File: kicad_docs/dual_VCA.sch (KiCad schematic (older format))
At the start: 18 parts, among them J1 signal_in_1, J2 CV_in_1, J3 signal_in_2, J4 CV_in_2, J5 signal_out_1, J6 signal_out_2, J8 Conn_01x06, J9 Conn_01x06

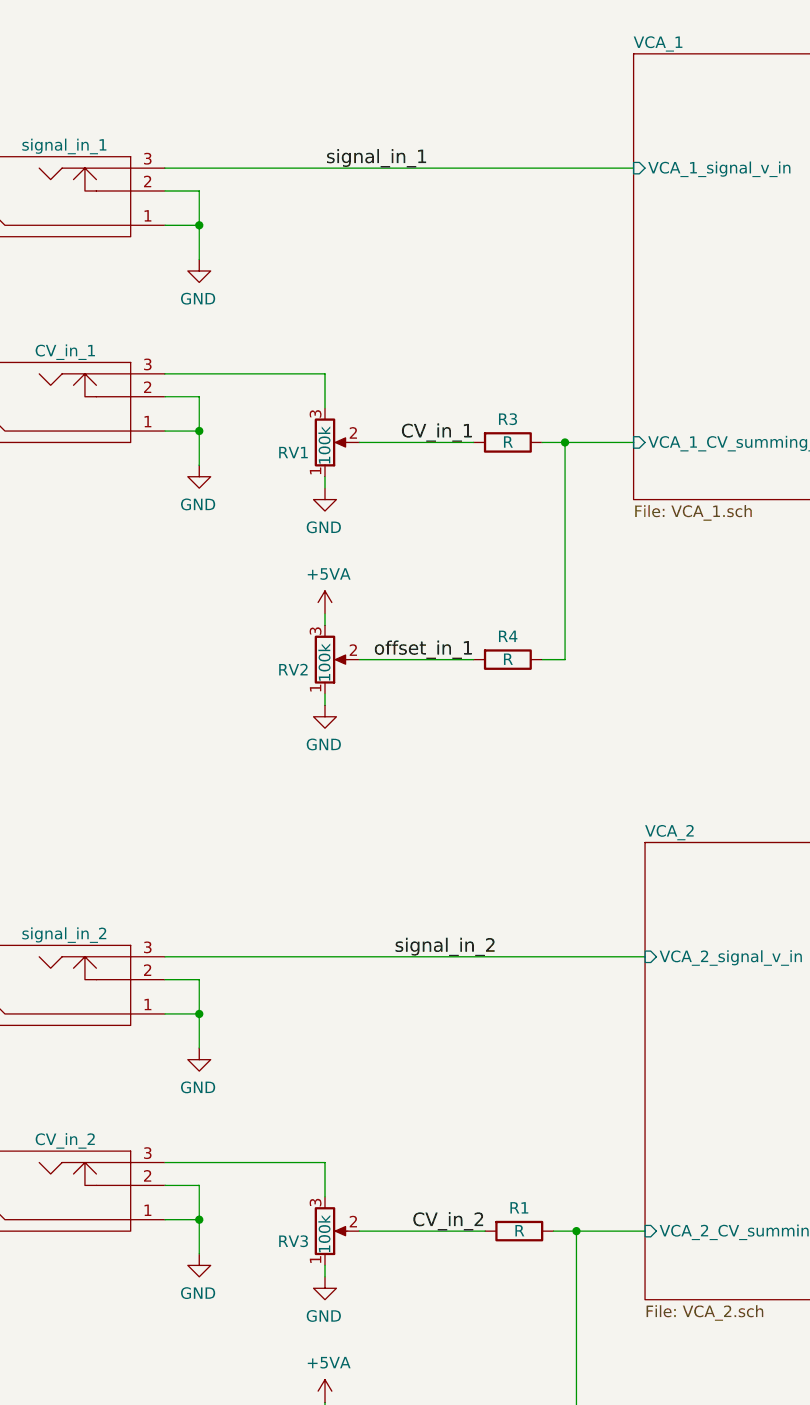
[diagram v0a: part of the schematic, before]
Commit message: add AC/DC coupling caps and jumper
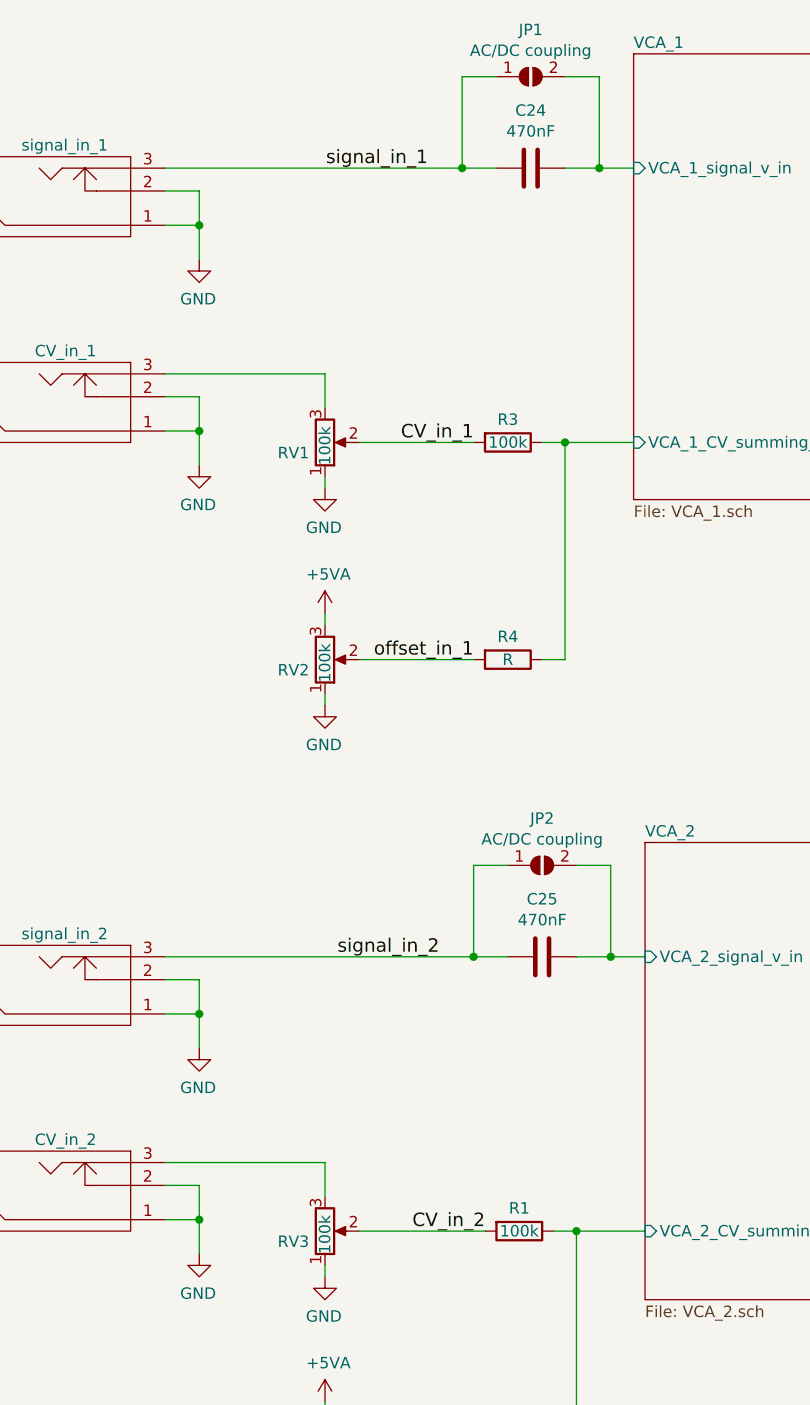
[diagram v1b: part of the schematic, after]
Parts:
- added C24, C25: 470nF, Capacitor_THT:C_Rect_L7.2mm_W3.5mm_P5.00mm_FKS2_FKP2_MKS2_MKP2, symbol Device:C
- added JP1, JP2: AC/DC coupling, Jumper:SolderJumper-2_P1.3mm_Open_RoundedPad1.0x1.5mm, symbol Jumper:SolderJumper_2_Open
- R1, R3: value R -> 100k
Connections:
- net signal_in_1: now also C24.2, JP1.1 (A)
- net signal_in_2: now also C25.2, JP2.1 (A)
- new net VCA_1/VCA_1_signal_v_in: C24.1, JP1.2 (B)
- new net VCA_2/VCA_2_signal_v_in: C25.1, JP2.2 (B)
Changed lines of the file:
@@
 Wire Wire Line
 	1700 5550 2400 5550
-Wire Wire Line
-	1700 4650 3800 4650
 $Comp
 L Device:R R1
@@
 P 3250 5850
 F 0 "R1" V 3150 5850 50  0000 C CNN
-F 1 "R" V 3250 5850 50  0000 C CNN
+F 1 "100k" V 3250 5850 50  0000 C CNN
 F 2 "Resistor_SMD:R_0805_2012Metric_Pad1.15x1.40mm_HandSolder" V 3180 5850 50  0001 C CNN
 F 3 "~" H 3250 5850 50  0001 C CNN
@@
 Wire Wire Line
 	2400 2100 2400 2250
-Wire Wire Line
-	1700 1200 3750 1200
 $Comp
 L Device:R R3
@@
 P 3200 2400
 F 0 "R3" V 3100 2400 50  0000 C CNN
-F 1 "R" V 3200 2400 50  0000 C CNN
+F 1 "100k" V 3200 2400 50  0000 C CNN
 F 2 "Resistor_SMD:R_0805_2012Metric_Pad1.15x1.40mm_HandSolder" V 3130 2400 50  0001 C CNN
 F 3 "~" H 3200 2400 50  0001 C CNN
@@
 Text Label 10250 1050 2    59   ~ 0
 signal_in_1
-Text Label 10250 1250 2    59   ~ 0
-CV_in_1
 Text Label 10250 1350 2    59   ~ 0
 offset_in_1
-Text Label 10250 1150 2    59   ~ 0
-signal_out_1
 $Comp
 L Connector_Generic:Conn_01x06 J9
@@
 Text Label 6750 1200 2    59   ~ 0
 signal_out_1
-Text Label 3150 4650 2    59   ~ 0
+Text Label 2900 4650 2    59   ~ 0
 signal_in_2
 Text Label 3100 5850 2    59   ~ 0
@@
 Wire Wire Line
 	6200 4650 6850 4650
+$Comp
+L Device:C C24
+U 1 1 5E401C22
+P 3300 1200
+F 0 "C24" V 3048 1200 50  0000 C CNN
+F 1 "470nF" V 3139 1200 50  0000 C CNN
+F 2 "Capacitor_THT:C_Rect_L7.2mm_W3.5mm_P5.00mm_FKS2_FKP2_MKS2_MKP2" H 3338 1050 50  0001 C CNN
+F 3 "~" H 3300 1200 50  0001 C CNN
+	1    3300 1200
+	0    1    1    0
+$EndComp
+Wire Wire Line
+	3450 1200 3600 1200
+Wire Wire Line
+	3150 1200 3000 1200
+$Comp
+L Jumper:SolderJumper_2_Open JP1
+U 1 1 5E4046A9
+P 3300 800
+F 0 "JP1" H 3300 1005 50  0000 C CNN
+F 1 "AC/DC coupling" H 3300 914 50  0000 C CNN
+F 2 "Jumper:SolderJumper-2_P1.3mm_Open_RoundedPad1.0x1.5mm" H 3300 800 50  0001 C CNN
+F 3 "~" H 3300 800 50  0001 C CNN
+	1    3300 800
+	1    0    0    -1
+$EndComp
+Wire Wire Line
+	3150 800  3000 800
+Wire Wire Line
+	3000 800  3000 1200
+Connection ~ 3000 1200
+Wire Wire Line
+	3000 1200 1700 1200
+Wire Wire Line
+	3450 800  3600 800
+Wire Wire Line
+	3600 800  3600 1200
+Connection ~ 3600 1200
+Wire Wire Line
+	3600 1200 3750 1200
+$Comp
+L Device:C C25
+U 1 1 5E409E9E
+P 3350 4650
+F 0 "C25" V 3098 4650 50  0000 C CNN
+F 1 "470nF" V 3189 4650 50  0000 C CNN
+F 2 "Capacitor_THT:C_Rect_L7.2mm_W3.5mm_P5.00mm_FKS2_FKP2_MKS2_MKP2" H 3388 4500 50  0001 C CNN
+F 3 "~" H 3350 4650 50  0001 C CNN
+	1    3350 4650
+	0    1    1    0
+$EndComp
+Wire Wire Line
+	3500 4650 3650 4650
+Wire Wire Line
+	3200 4650 3050 4650
+$Comp
+L Jumper:SolderJumper_2_Open JP2
+U 1 1 5E409EA6
+P 3350 4250
+F 0 "JP2" H 3350 4455 50  0000 C CNN
+F 1 "AC/DC coupling" H 3350 4364 50  0000 C CNN
+F 2 "Jumper:SolderJumper-2_P1.3mm_Open_RoundedPad1.0x1.5mm" H 3350 4250 50  0001 C CNN
+F 3 "~" H 3350 4250 50  0001 C CNN
+	1    3350 4250
+	1    0    0    -1
+$EndComp
+Wire Wire Line
+	3200 4250 3050 4250
+Wire Wire Line
+	3050 4250 3050 4650
+Connection ~ 3050 4650
+Wire Wire Line
+	3050 4650 1700 4650
+Wire Wire Line
+	3500 4250 3650 4250
+Wire Wire Line
+	3650 4250 3650 4650
+Connection ~ 3650 4650
+Wire Wire Line
+	3650 4650 3800 4650
+Text Label 10250 1250 2    59   ~ 0
+CV_in_1
+Text Label 10250 1150 2    59   ~ 0
+signal_out_1
 $EndSCHEMATC

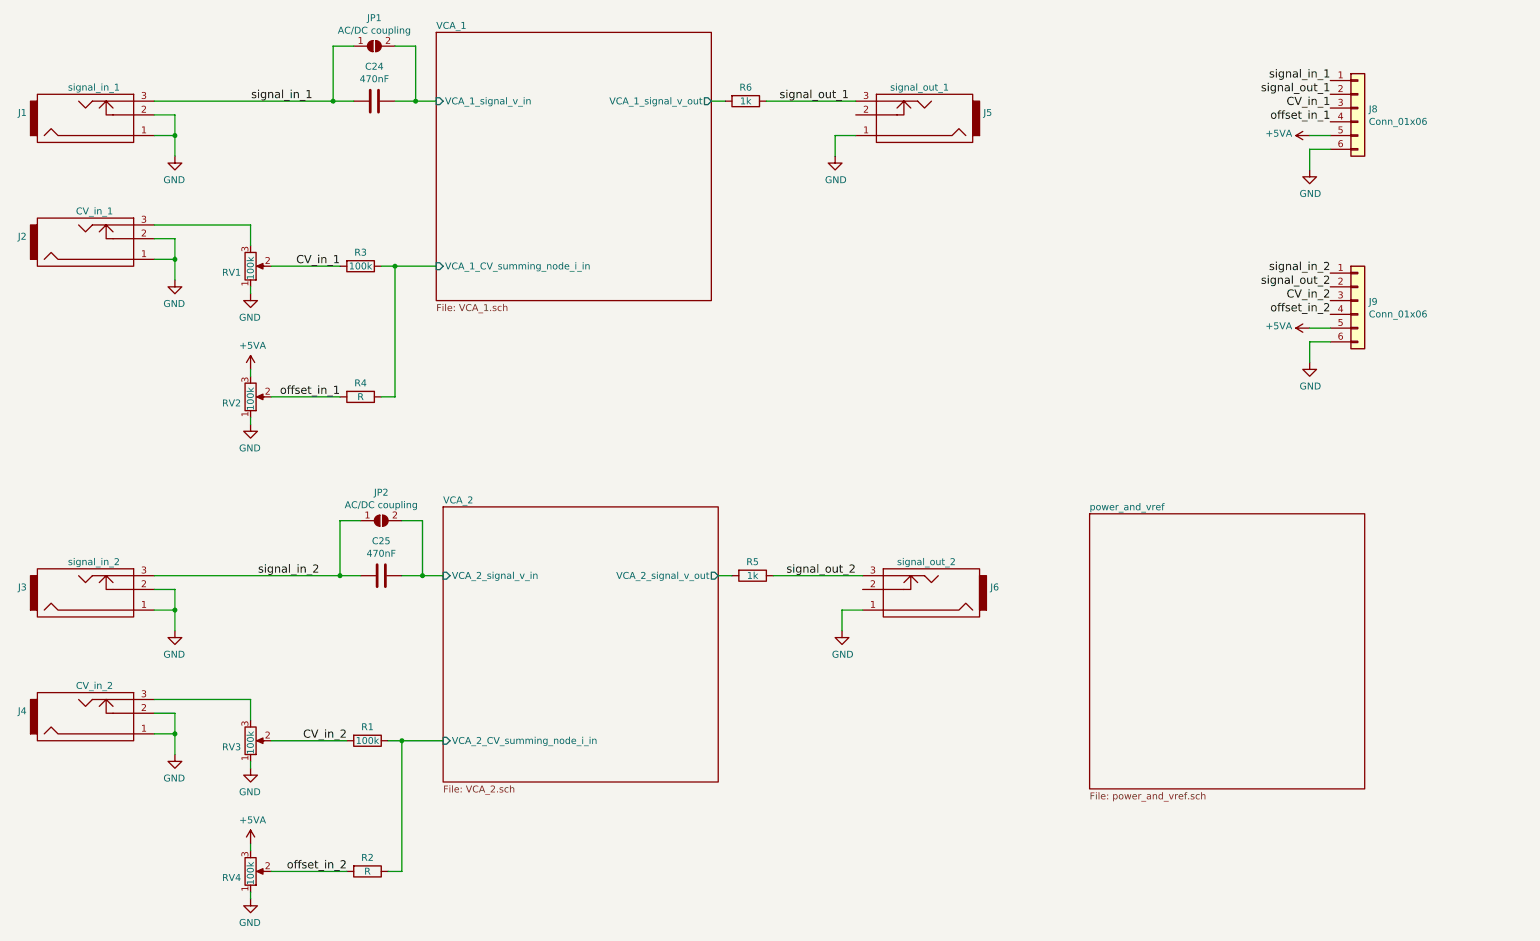
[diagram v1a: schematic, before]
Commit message: add values to r's, add r's to CV circuit
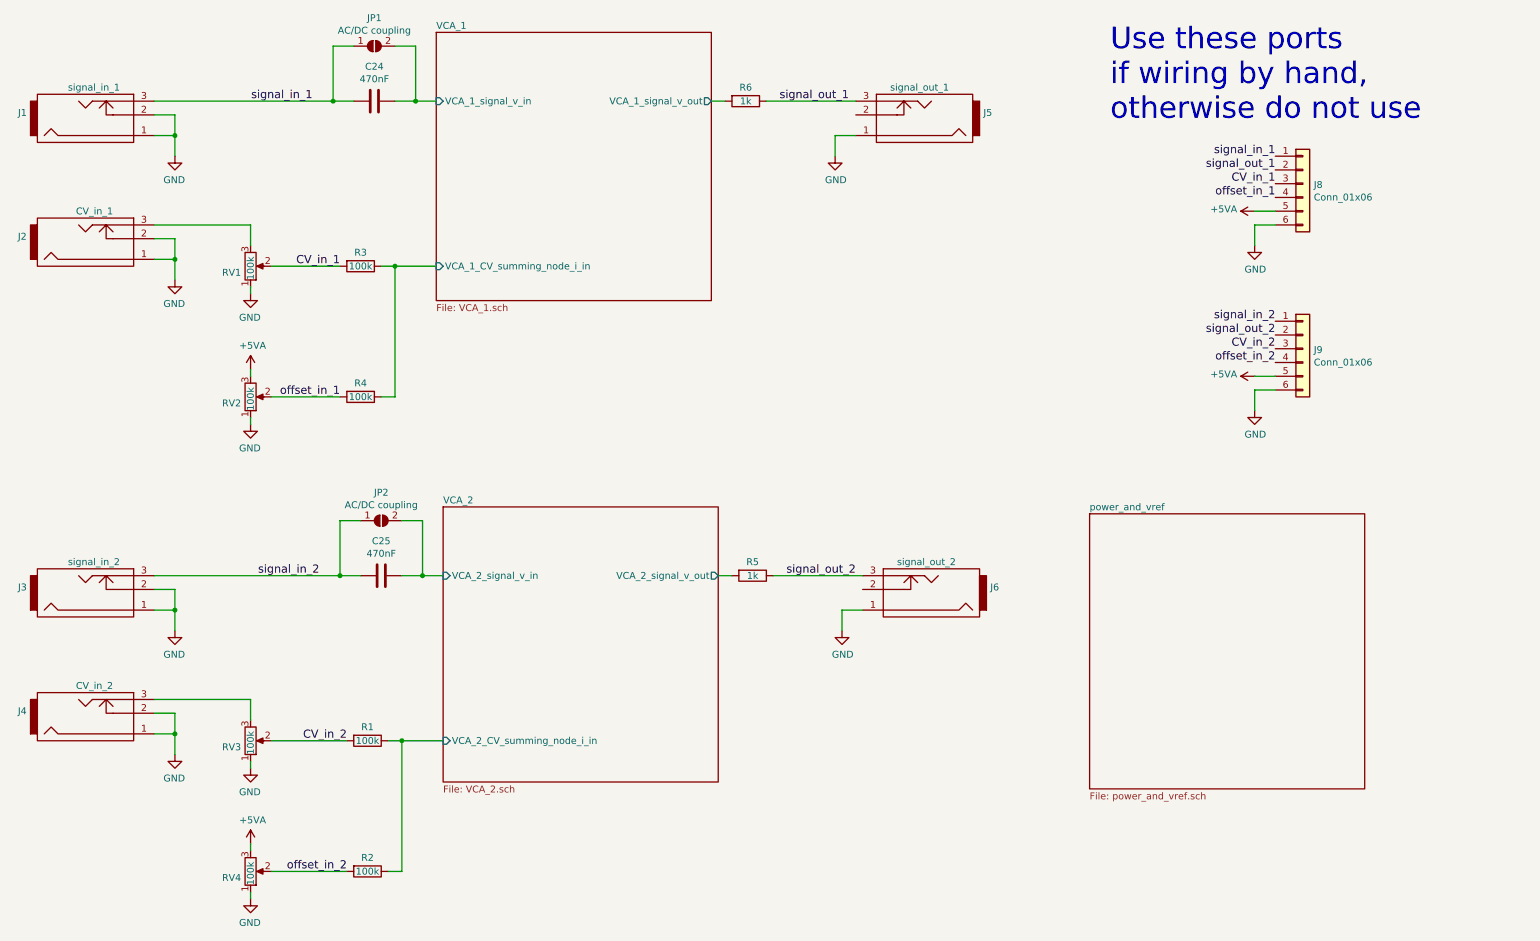
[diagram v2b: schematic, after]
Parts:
- R2, R4: value R -> 100k
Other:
- note added: "Use these ports \nif wiring by hand,\notherwise do not use"
- moved on the sheet: J8, J9
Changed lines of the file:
@@
 P 3250 6800
 F 0 "R2" V 3150 6800 50  0000 C CNN
-F 1 "R" V 3250 6800 50  0000 C CNN
+F 1 "100k" V 3250 6800 50  0000 C CNN
 F 2 "Resistor_SMD:R_0805_2012Metric_Pad1.15x1.40mm_HandSolder" V 3180 6800 50  0001 C CNN
 F 3 "~" H 3250 6800 50  0001 C CNN
@@
 P 3200 3350
 F 0 "R4" V 3100 3350 50  0000 C CNN
-F 1 "R" V 3200 3350 50  0000 C CNN
+F 1 "100k" V 3200 3350 50  0000 C CNN
 F 2 "Resistor_SMD:R_0805_2012Metric_Pad1.15x1.40mm_HandSolder" V 3130 3350 50  0001 C CNN
 F 3 "~" H 3200 3350 50  0001 C CNN
@@
 L Connector_Generic:Conn_01x06 J8
 U 1 1 5EBCF2F2
-P 10450 1250
-F 0 "J8" H 10530 1242 50  0000 L CNN
-F 1 "Conn_01x06" H 10530 1151 50  0000 L CNN
-F 2 "Connector_PinHeader_2.54mm:PinHeader_1x06_P2.54mm_Vertical" H 10450 1250 50  0001 C CNN
-F 3 "~" H 10450 1250 50  0001 C CNN
-	1    10450 1250
+P 10050 1800
+F 0 "J8" H 10130 1792 50  0000 L CNN
+F 1 "Conn_01x06" H 10130 1701 50  0000 L CNN
+F 2 "Connector_PinHeader_2.54mm:PinHeader_1x06_P2.54mm_Vertical" H 10050 1800 50  0001 C CNN
+F 3 "~" H 10050 1800 50  0001 C CNN
+	1    10050 1800
 	1    0    0    -1
 $EndComp
@@
 L power:GND #PWR012
 U 1 1 5EBD0AF7
-P 10100 1700
-F 0 "#PWR012" H 10100 1450 50  0001 C CNN
-F 1 "GND" H 10105 1527 50  0000 C CNN
-F 2 "" H 10100 1700 50  0001 C CNN
-F 3 "" H 10100 1700 50  0001 C CNN
-	1    10100 1700
-	1    0    0    -1
-$EndComp
-Wire Wire Line
-	10100 1700 10100 1550
-Wire Wire Line
-	10100 1550 10250 1550
+P 9700 2250
+F 0 "#PWR012" H 9700 2000 50  0001 C CNN
+F 1 "GND" H 9705 2077 50  0000 C CNN
+F 2 "" H 9700 2250 50  0001 C CNN
+F 3 "" H 9700 2250 50  0001 C CNN
+	1    9700 2250
+	1    0    0    -1
+$EndComp
+Wire Wire Line
+	9700 2250 9700 2100
+Wire Wire Line
+	9700 2100 9850 2100
 $Comp
 L power:+5VA #PWR011
 U 1 1 5EBD3357
-P 10100 1450
-F 0 "#PWR011" H 10100 1300 50  0001 C CNN
-F 1 "+5VA" V 10115 1577 50  0000 L CNN
-F 2 "" H 10100 1450 50  0001 C CNN
-F 3 "" H 10100 1450 50  0001 C CNN
-	1    10100 1450
+P 9700 2000
+F 0 "#PWR011" H 9700 1850 50  0001 C CNN
+F 1 "+5VA" V 9715 2127 50  0000 L CNN
+F 2 "" H 9700 2000 50  0001 C CNN
+F 3 "" H 9700 2000 50  0001 C CNN
+	1    9700 2000
 	0    -1   -1   0
 $EndComp
 Wire Wire Line
-	10100 1450 10250 1450
-Text Label 10250 1050 2    59   ~ 0
+	9700 2000 9850 2000
+Text Label 9850 1600 2    59   ~ 0
 signal_in_1
-Text Label 10250 1350 2    59   ~ 0
+Text Label 9850 1900 2    59   ~ 0
 offset_in_1
 $Comp
 L Connector_Generic:Conn_01x06 J9
 U 1 1 5EBD8F81
-P 10450 2650
-F 0 "J9" H 10530 2642 50  0000 L CNN
-F 1 "Conn_01x06" H 10530 2551 50  0000 L CNN
-F 2 "Connector_PinHeader_2.54mm:PinHeader_1x06_P2.54mm_Vertical" H 10450 2650 50  0001 C CNN
-F 3 "~" H 10450 2650 50  0001 C CNN
-	1    10450 2650
+P 10050 3000
+F 0 "J9" H 10130 2992 50  0000 L CNN
+F 1 "Conn_01x06" H 10130 2901 50  0000 L CNN
+F 2 "Connector_PinHeader_2.54mm:PinHeader_1x06_P2.54mm_Vertical" H 10050 3000 50  0001 C CNN
+F 3 "~" H 10050 3000 50  0001 C CNN
+	1    10050 3000
 	1    0    0    -1
 $EndComp
@@
 L power:GND #PWR014
 U 1 1 5EBD8F87
-P 10100 3100
-F 0 "#PWR014" H 10100 2850 50  0001 C CNN
-F 1 "GND" H 10105 2927 50  0000 C CNN
-F 2 "" H 10100 3100 50  0001 C CNN
-F 3 "" H 10100 3100 50  0001 C CNN
-	1    10100 3100
-	1    0    0    -1
-$EndComp
-Wire Wire Line
-	10100 3100 10100 2950
-Wire Wire Line
-	10100 2950 10250 2950
+P 9700 3450
+F 0 "#PWR014" H 9700 3200 50  0001 C CNN
+F 1 "GND" H 9705 3277 50  0000 C CNN
+F 2 "" H 9700 3450 50  0001 C CNN
+F 3 "" H 9700 3450 50  0001 C CNN
+	1    9700 3450
+	1    0    0    -1
+$EndComp
+Wire Wire Line
+	9700 3450 9700 3300
+Wire Wire Line
+	9700 3300 9850 3300
 $Comp
 L power:+5VA #PWR013
 U 1 1 5EBD8F8F
-P 10100 2850
-F 0 "#PWR013" H 10100 2700 50  0001 C CNN
-F 1 "+5VA" V 10115 2977 50  0000 L CNN
-F 2 "" H 10100 2850 50  0001 C CNN
-F 3 "" H 10100 2850 50  0001 C CNN
-	1    10100 2850
+P 9700 3200
+F 0 "#PWR013" H 9700 3050 50  0001 C CNN
+F 1 "+5VA" V 9715 3327 50  0000 L CNN
+F 2 "" H 9700 3200 50  0001 C CNN
+F 3 "" H 9700 3200 50  0001 C CNN
+	1    9700 3200
 	0    -1   -1   0
 $EndComp
 Wire Wire Line
-	10100 2850 10250 2850
-Text Label 10250 2450 2    59   ~ 0
+	9700 3200 9850 3200
+Text Label 9850 2800 2    59   ~ 0
 signal_in_2
-Text Label 10250 2650 2    59   ~ 0
+Text Label 9850 3000 2    59   ~ 0
 CV_in_2
-Text Label 10250 2750 2    59   ~ 0
+Text Label 9850 3100 2    59   ~ 0
 offset_in_2
-Text Label 10250 2550 2    59   ~ 0
+Text Label 9850 2900 2    59   ~ 0
 signal_out_2
 Text Label 2850 1200 2    59   ~ 0
@@
 Wire Wire Line
 	3650 4650 3800 4650
-Text Label 10250 1250 2    59   ~ 0
+Text Label 9850 1800 2    59   ~ 0
 CV_in_1
-Text Label 10250 1150 2    59   ~ 0
+Text Label 9850 1700 2    59   ~ 0
 signal_out_1
+Text Notes 8650 1350 0    157  ~ 0
+Use these ports \nif wiring by hand,\notherwise do not use
 $EndSCHEMATC
